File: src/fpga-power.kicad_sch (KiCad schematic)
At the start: 21 parts

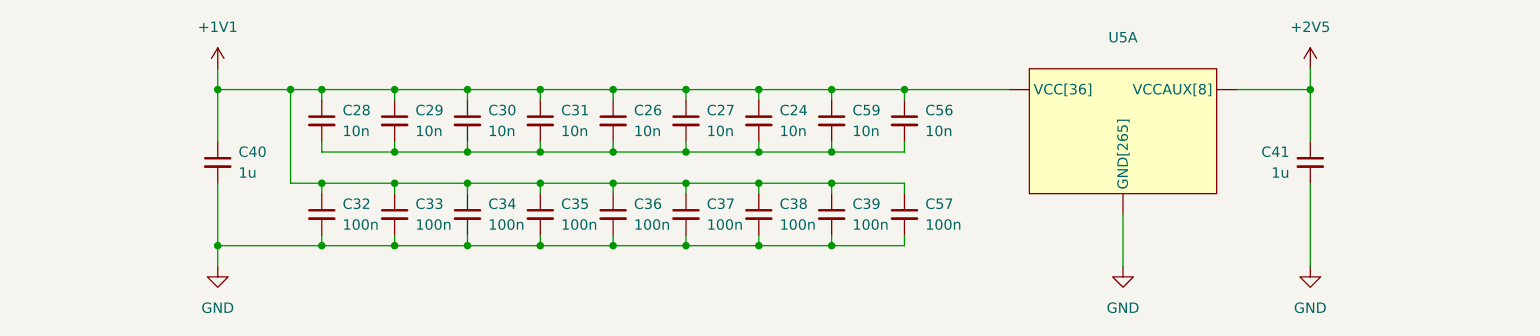
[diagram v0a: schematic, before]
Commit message: Updates the fpga configuration schematic
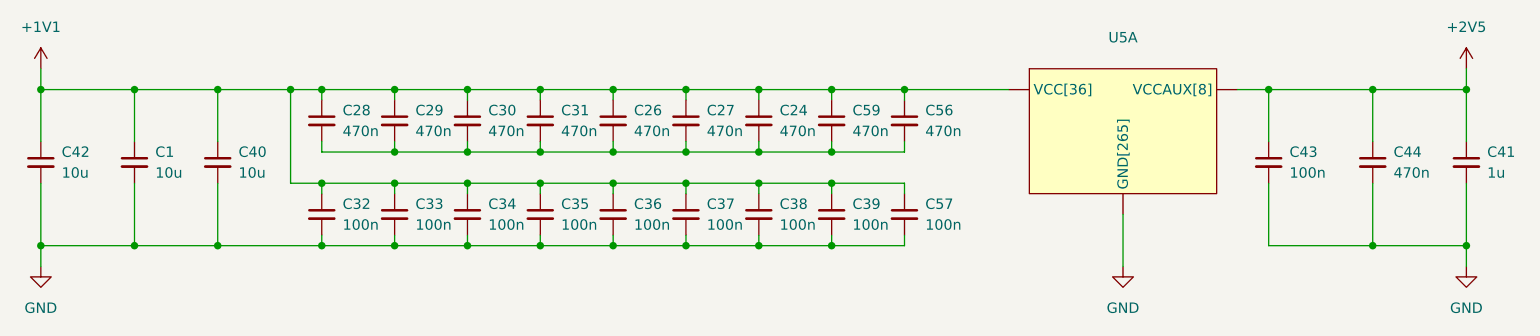
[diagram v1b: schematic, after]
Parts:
- added C1, C42: 10u, symbol Device:C_Small
- added C43: 100n, symbol Device:C_Small
- added C44: 470n, symbol Device:C_Small
- C24, C26, C27, C28, C29, C30, C31, C56, C59: value 10n -> 470n
- C40: value 1u -> 10u
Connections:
- net +1V1: now also C1.1, C42.1
- net +2V5: now also C43.1, C44.1
- net GND: now also C1.2, C42.2, C43.2, C44.2
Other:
- moved on the sheet: C41

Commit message: Adds symbol for DDR2
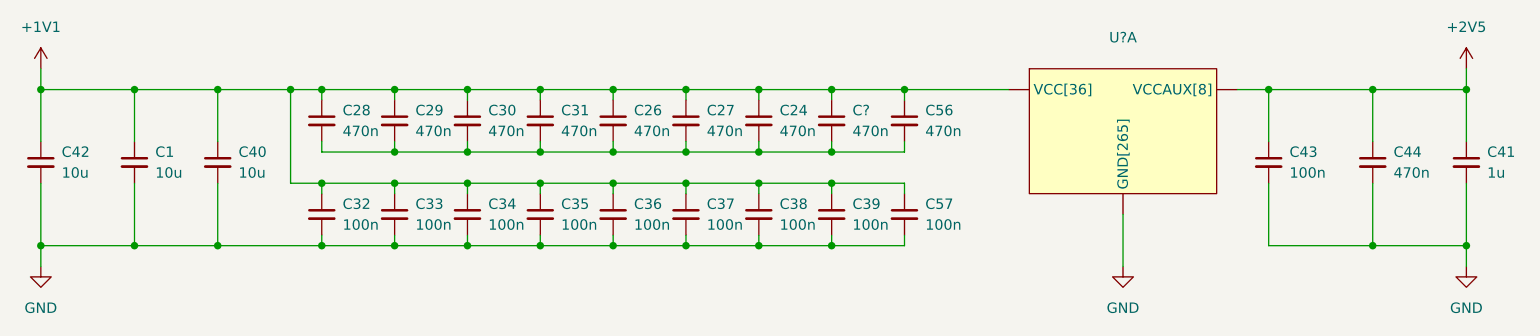
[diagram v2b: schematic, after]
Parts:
- renumbered C59 to C?, U5 to U?
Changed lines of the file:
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@@
 		(dnp no)
 		(fields_autoplaced yes)
-		(property "Reference" "#PWR028"
+		(property "Reference" "#PWR?"
 			(at 229.87 85.09 0)
 			(effects
@@
 		)
 		(pin "1"
+		)
+		(instances
+			(project "ecap5-bsom"
+				(path "/c5fd18a3-9aa0-4151-b6e0-94da3d606686/93025bf8-f1b9-4669-843e-f0f0cbaf67cc"
+					(reference "#PWR?")
+					(unit 1)
+				)
+			)
 		)
 	)
@@
 		(dnp no)
 		(fields_autoplaced yes)
-		(property "Reference" "U5"
+		(property "Reference" "U?"
 			(at 187.96 77.47 0)
 			(effects
@@
 		)
 		(pin "AA13"
+		)
+		(instances
+			(project "ecap5-bsom"
+				(path "/c5fd18a3-9aa0-4151-b6e0-94da3d606686/93025bf8-f1b9-4669-843e-f0f0cbaf67cc"
+					(reference "U?")
+					(unit 1)
+				)
+			)
 		)
 	)
@@
 		(dnp no)
 		(fields_autoplaced yes)
-		(property "Reference" "#PWR027"
+		(property "Reference" "#PWR?"
 			(at 187.96 111.76 0)
 			(effects
@@
 		)
 		(pin "1"
+		)
+		(instances
+			(project "ecap5-bsom"
+				(path "/c5fd18a3-9aa0-4151-b6e0-94da3d606686/93025bf8-f1b9-4669-843e-f0f0cbaf67cc"
+					(reference "#PWR?")
+					(unit 1)
+				)
+			)
 		)
 	)
@@
 		(dnp no)
 		(fields_autoplaced yes)
-		(property "Reference" "C59"
+		(property "Reference" "C?"
 			(at 154.94 86.3662 0)
 			(effects
@@
 		)
 		(pin "1"
+		)
+		(instances
+			(project "ecap5-bsom"
+				(path "/c5fd18a3-9aa0-4151-b6e0-94da3d606686/93025bf8-f1b9-4669-843e-f0f0cbaf67cc"
+					(reference "C?")
+					(unit 1)
+				)
+			)
 		)
 	)
@@
 		(dnp no)
 		(fields_autoplaced yes)
-		(property "Reference" "#PWR022"
+		(property "Reference" "#PWR?"
 			(at 55.88 85.09 0)
 			(effects
@@
 		(pin "1"
 		)
-	)
+		(instances
+			(project "ecap5-bsom"
+				(path "/c5fd18a3-9aa0-4151-b6e0-94da3d606686/93025bf8-f1b9-4669-843e-f0f0cbaf67cc"
+					(reference "#PWR?")
+					(unit 1)
+				)
+			)
+		)
+	)
